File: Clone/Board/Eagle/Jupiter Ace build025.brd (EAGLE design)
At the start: 209 x 184 mm, 325 parts, among them K1 1, K10 0, K11 Q, K12 W, K13 E, K14 R, K15 T, K16 Y, K17 U, K18 I, K19 O, K2 2, K20 P, K21 A, K22 S, K23 D, K24 F, K25 G, K26 H, K27 J, K28 K, K29 L, K3 3, K30 ENTER, K31 SHIFT, K32 SYMBOL, K33 Z, K34 X, K35 C, K36 V, K37 B, K38 N, K39 M, K4 4, K40 SPACE, K41 SPACE, K5 5, K6 6, K7 7, K8 8, K9 9, Q1 2N3904, Q3 BC337, U1 7805, U2 MAX4390EUK, X1 6.5MHz, X2 CON-CONRAD_736880-49

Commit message: build 25
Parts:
- added C23: 10pF, rcl:C025-025X050
- added JP11, JP12: (no value), pinhead:2X05
- added JP14: (no value), pinhead:1X01
- added JP16: (no value), pinhead:2X08
- added JP17, JP18: (no value), pinhead:1X02
- added JP2, JP9: (no value), pinhead:1X20
- added R44: 1K, pot:B25P
- R21, R22, R23: device rcl:0204/7 -> rcl:0204V
- moved Z29 8.89 mm to (59.7, 113.0)
- moved Z30 7.62 mm to (58.4, 134.6)
- moved R23 6.53 mm to (140.8, 118.2)
- moved R21 6.35 mm to (141.0, 110.5)
- moved R22 6.35 mm to (141.0, 115.6)
- moved Z26 6.35 mm to (82.5, 100.3)
- moved D11 5.24 mm to (101.6, 141.0)
- moved R204 5.24 mm to (141.0, 97.8)
- moved R202 5.24 mm to (118.1, 97.8)
- moved Z22 5.24 mm to (156.2, 127.0)
- moved R203 5.24 mm to (141.0, 95.2)
- moved R205 5.24 mm to (141.0, 100.3)
- moved R206 5.24 mm to (141.0, 102.9)
- moved R200 5.24 mm to (118.1, 102.9)
- moved R201 5.24 mm to (118.1, 100.3)
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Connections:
- net N$52 renamed CNT3'
- net N$53 renamed CNT14'
- net N$54 renamed CNT13'
- net N$55 renamed CNT12'
- net N$79 renamed CNT7'
- net N$87 renamed CNT6'
- net N$88 renamed CNT5'
- net N$89 renamed CNT4'
- net N$90 renamed CNT15'
- net N$92 renamed CNT16'
- new net N$33: C23.2, R44.A, Z28.7
- new net N$57: JP11.8, Z5-6.9
- new net N$62: JP11.4, Z5-6.7
- new net N$66: JP11.2, Z5-6.6
- new net N$67: JP11.6, Z5-6.8
- new net N$68: JP11.10, Z5-6.10
- new net N$69: JP12.8, Z7-8.9
- new net N$71: JP12.2, Z7-8.6
- new net N$82: JP12.4, Z7-8.7
- new net N$84: JP12.6, Z7-8.8
- new net N$85: JP12.10, Z7-8.10
- new net N$91: JP17.1, R23.1
- net /BUSAK: now also JP9.18
- net /BUSRQ: now also JP9.16
- net /HALT: now also JP2.18
- net /INT: now also JP2.16
- net /IORQ: now also JP2.20
- net /M1: now also JP9.14
- net /MREQ: now also JP2.19
- net /NMI: now also JP2.17
- net /RD: now also JP9.20
- net /RFSH: now also JP9.13
- net /WAIT: now also JP9.17
- net /WR: now also JP9.19
- net A0: now also JP9.11
- net A1: now also JP9.10
- net A10: now also JP9.1
- net A11: now also JP2.1
- net A12: now also JP2.2
- net A13: now also JP2.3
- net A14: now also JP2.4
- net A15: now also JP2.5
- net A2: now also JP9.9
- net A3: now also JP9.8
- net A4: now also JP9.7
- net A5: now also JP9.6
- net A6: now also JP9.5
- net A7: now also JP9.4
- net A8: now also JP9.3
- net A9: now also JP9.2
- net CLK: now also R44.E, R44.S; no longer Z28.7
- net CNT10: now also JP18.1
- net CNT11: now also JP17.2; no longer R23.1
- net CNT9: now also JP18.2
- net D0: now also JP2.14
- net D1: now also JP2.15
- net D2: now also JP2.12
- net D3: now also JP2.8
- net D4: now also JP2.7
- net D5: now also JP2.9
- net D6: now also JP2.10
- net D7: now also JP2.13
- net GND: now also C23.1, JP11.1, JP11.3, JP11.5, JP11.7, JP11.9, JP12.1, JP12.3, JP12.5, JP12.7, JP12.9, JP9.12; no longer Z5-6.10, Z5-6.6, Z5-6.7, Z5-6.8, Z5-6.9, Z7-8.10, Z7-8.6, Z7-8.7, Z7-8.8, Z7-8.9
- net KB: now also JP16.12, JP16.5
- net KC: now also JP16.7
- net KEYB2: now also JP16.2, SJ2.2
- net KEYB3: now also JP16.4, SJ3.2
- net KEYB4: now also JP16.6, SJ4.2
- net KEYB5: now also JP16.8, SJ5.2
- net KM: now also JP16.1
- net KN: now also JP16.3, JP16.9
- net KX: now also JP16.11
- net KZ: now also JP16.10
- net N$101: no longer SJ8.2
- net N$112: no longer SJ5.2
- net N$32: no longer SJ9.2
- net N$46: no longer SJ4.2
- net N$50: no longer SJ2.2
- net N$51: no longer SJ3.2
- net N$59: now also JP14.1
- net PHI: now also JP2.6
- net RESET: now also JP9.15
- net ROW1: now also JP16.13
- net ROW8: now also JP16.15
- net ROW_SS: now also JP16.14, SJ8.2
- net ROW_V: now also JP16.16, SJ9.2
- net VCC: now also JP2.11
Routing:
- net ROW_SS: track 32.5 -> 325.0 mm, vias 0 -> 3
- net ROW_V: track 50.2 -> 292.8 mm, vias 0 -> 3
- net KC: track 110.8 -> 243.6 mm, vias 1 -> 10
- net KZ: track 86.3 -> 214.2 mm, vias 1 -> 5
- net N$86: track 298.0 -> 171.9 mm, vias 4 -> 6
- net KEYB5: track 380.2 -> 500.6 mm
- net KX: track 93.1 -> 208.3 mm, vias 0 -> 4
- net GND: track 1385.2 -> 1272.2 mm, vias 17 -> 20
- net KEYB4: track 351.2 -> 448.0 mm, vias 1 -> 4
- net KN: track 174.9 -> 266.9 mm, vias 2 -> 3
- net /INT: track 229.5 -> 318.0 mm
- net KB: track 171.0 -> 256.7 mm, vias 2 -> 3
- net KM: track 191.5 -> 273.1 mm, vias 2 -> 10
- net VCC: track 1127.4 -> 1046.3 mm, vias 24 -> 20
- net KEYB3: track 394.3 -> 466.8 mm, vias 0 -> 5
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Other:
- board text added: "2022 Alejandro Valero Sebastián & Pedro Gimeno Fortea Mercury Ace v1.0 (Build 25)"
- board text removed: "2022 Alejandro Valero Sebastián & Pedro Gimeno Fortea Mercury Ace v1.0 (Build 23)"

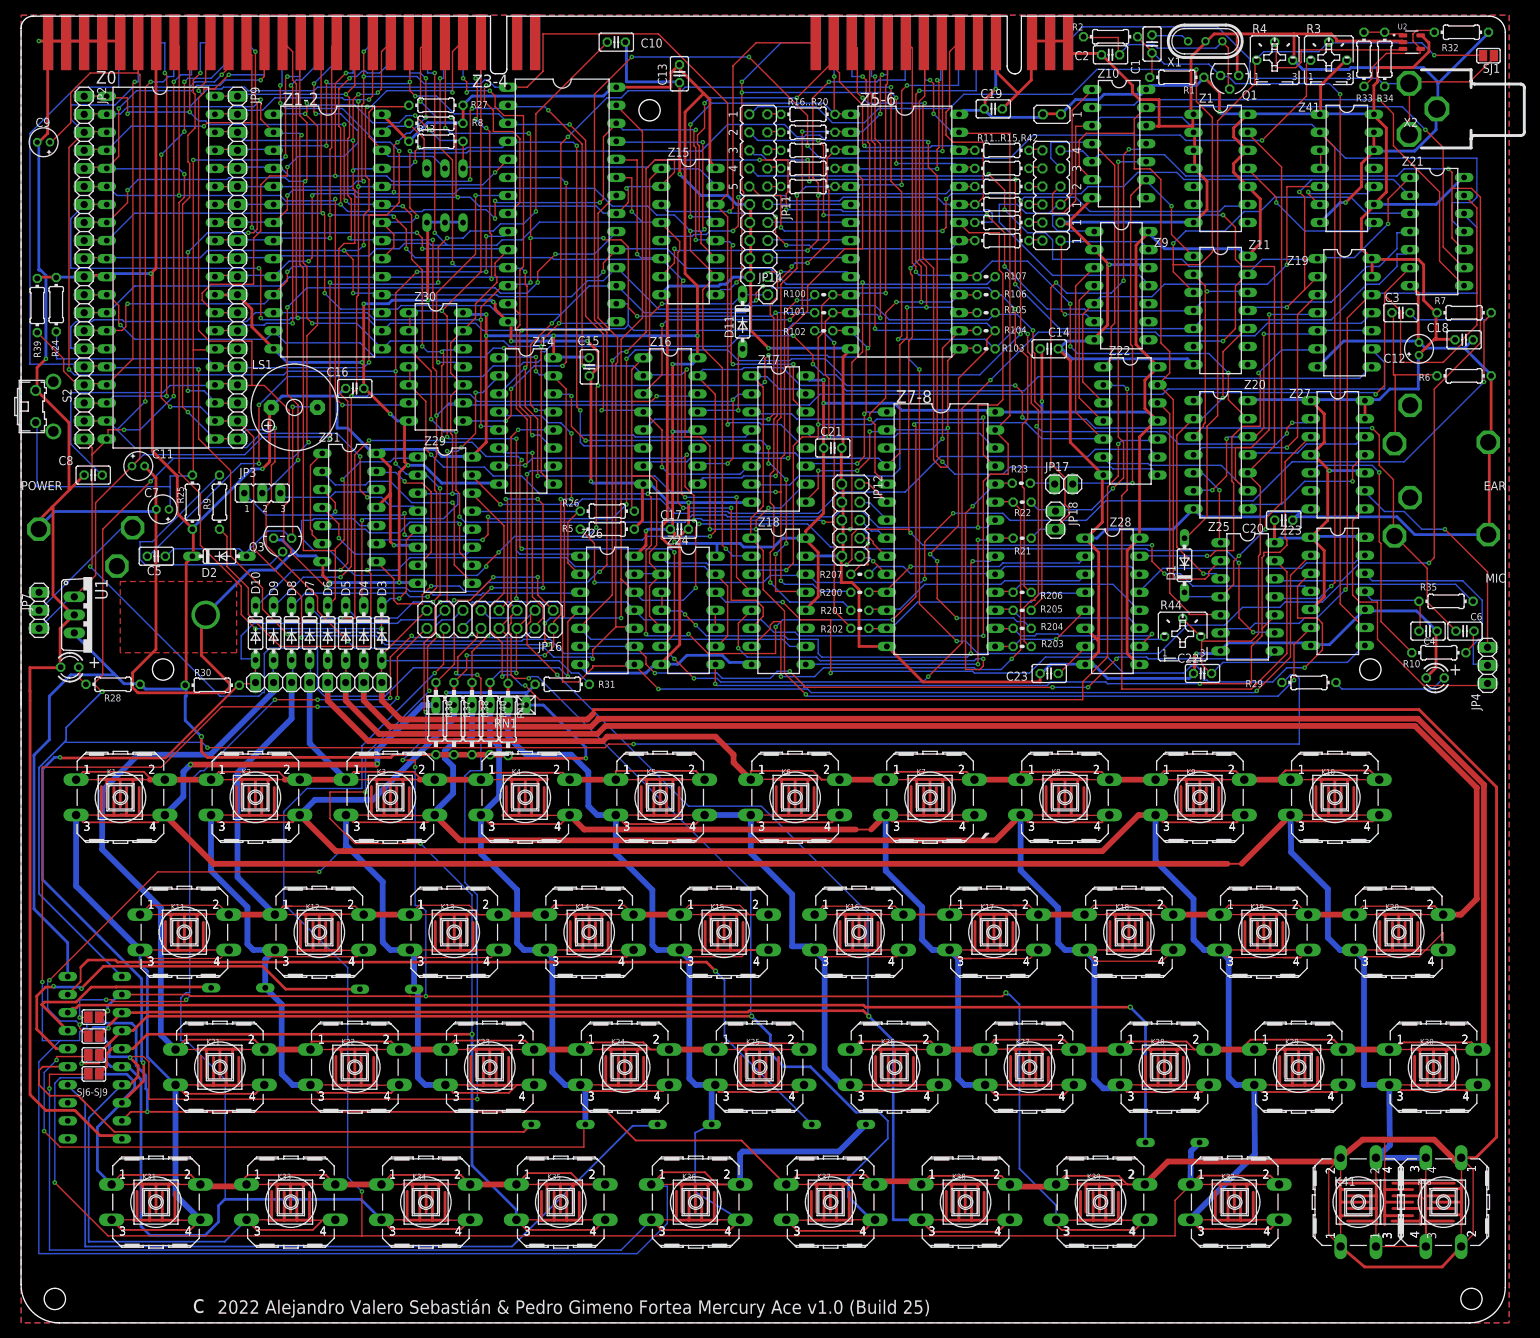
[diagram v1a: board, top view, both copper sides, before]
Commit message: capture inv bit
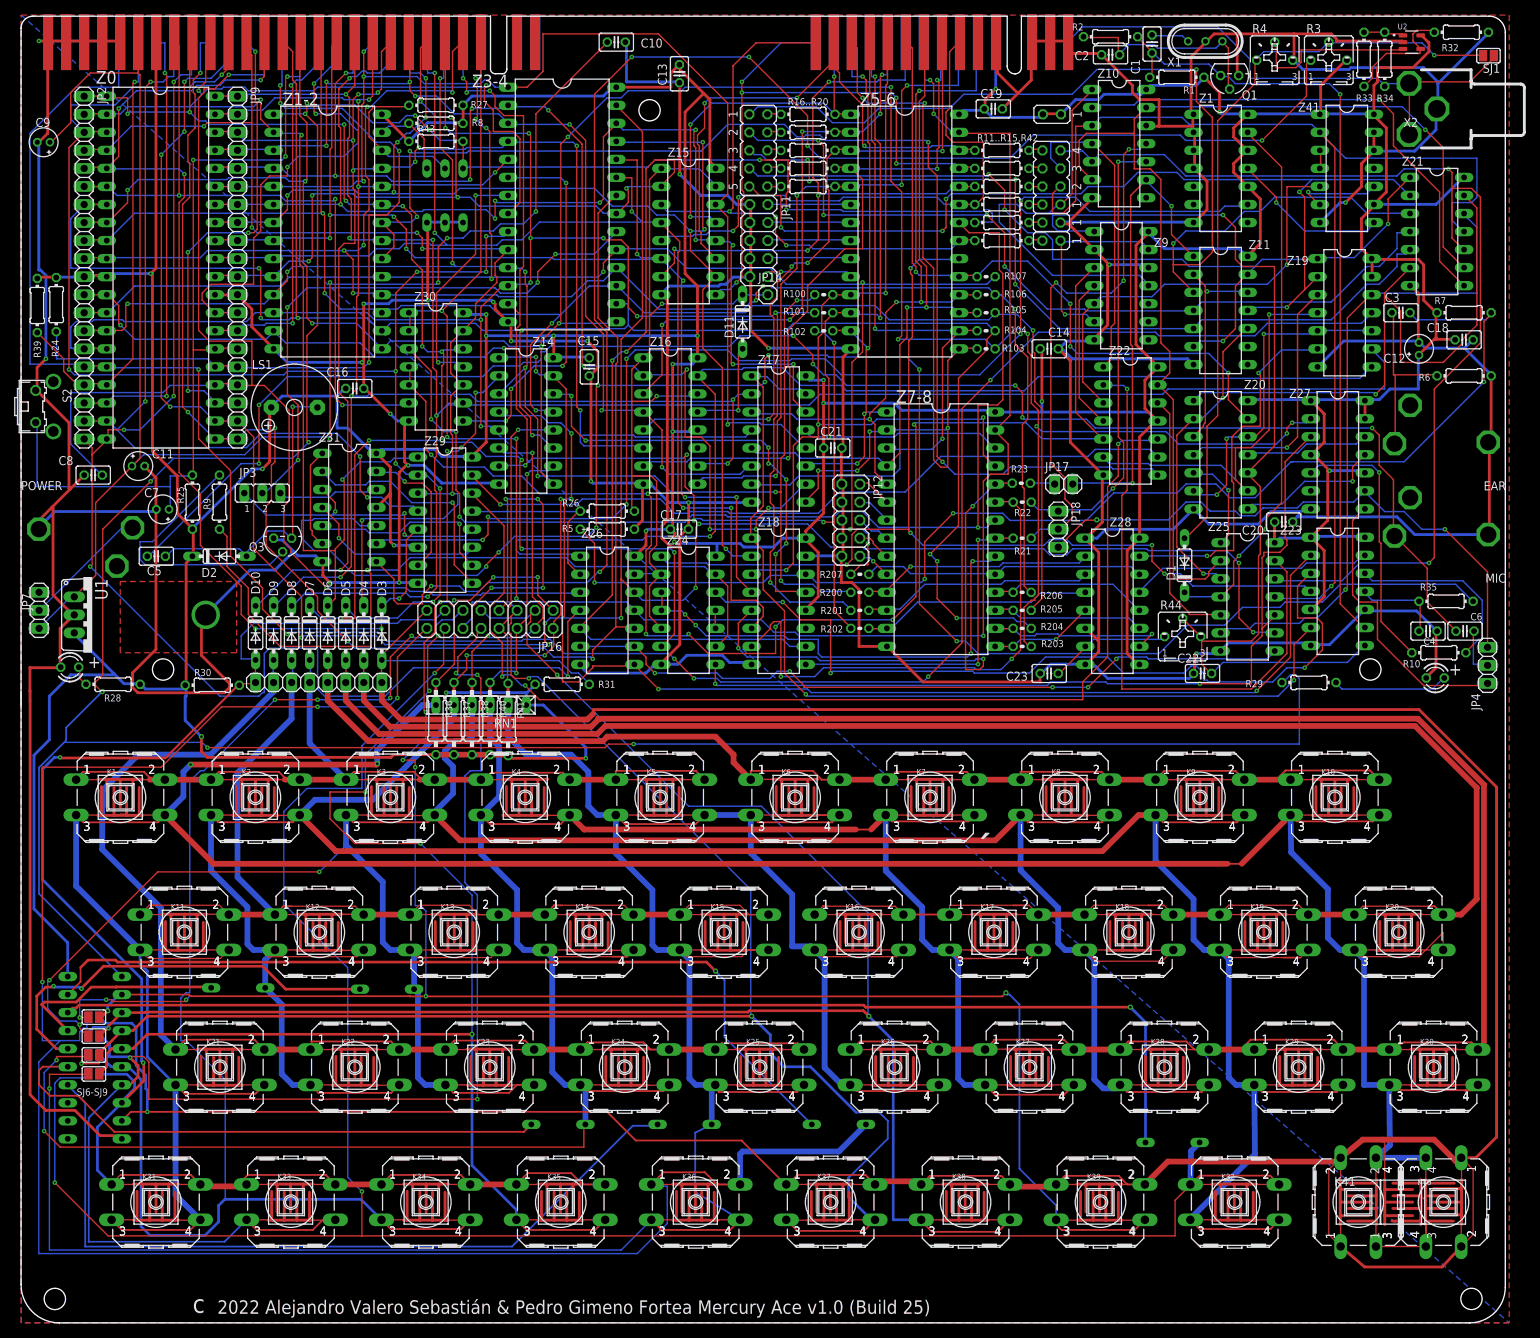
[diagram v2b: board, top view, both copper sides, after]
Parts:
- JP18: device pinhead:1X02 -> pinhead:1X03
- moved JP18 1.33 mm to (146.1, 111.8)
- moved C20 0.25 mm to (177.8, 112.8)
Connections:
- removed net N$15: JP4.1, Z27.9
- new net INV_BIT: JP18.3, JP4.1, Z27.9
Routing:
- net INV_BIT: track 0.00 -> 81.3 mm, vias 0 -> 2
- net N$15: track 32.7 -> 0.00 mm, vias 1 -> 0
- net N$11: track 12.1 -> 13.8 mm
- net N$28: track 172.8 -> 174.4 mm
- net VIDEN: track 45.4 -> 46.6 mm
- net CNT9: track 73.2 -> 74.2 mm
- net GND: track 1272.2 -> 1273.2 mm
- net /WR: track 340.5 -> 341.2 mm
- net N$30: track 145.7 -> 146.3 mm
